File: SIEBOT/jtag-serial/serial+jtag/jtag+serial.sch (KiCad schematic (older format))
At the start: 26 parts, among them J1 USB_2, K1 CONN_3, K2 CONN_3, P1 CONN_14, P2 CONN_14, U1 93LC46BT-I/OT, U2 FT2232D, X1 CRYSTAL

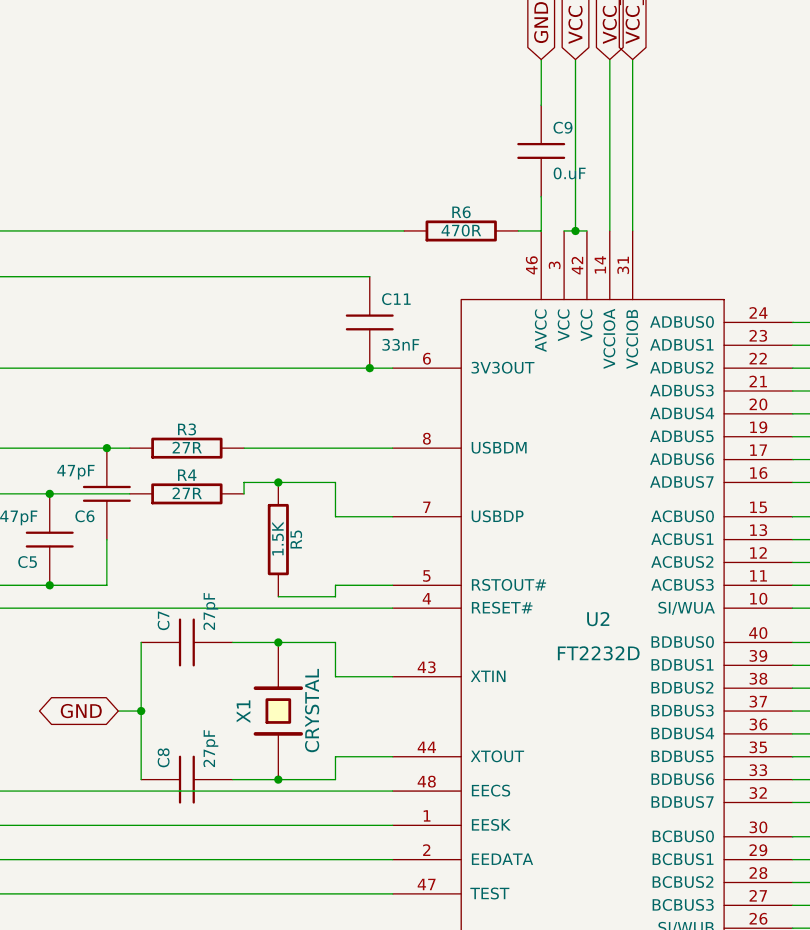
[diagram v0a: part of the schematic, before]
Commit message: Agregada BOM con referencias a Digikey. Corregido enpaquetado ferrita y valores condensadores carga del cristal. Signed-off-by: Erwin Lopez <erwinkendo@gmail.com>
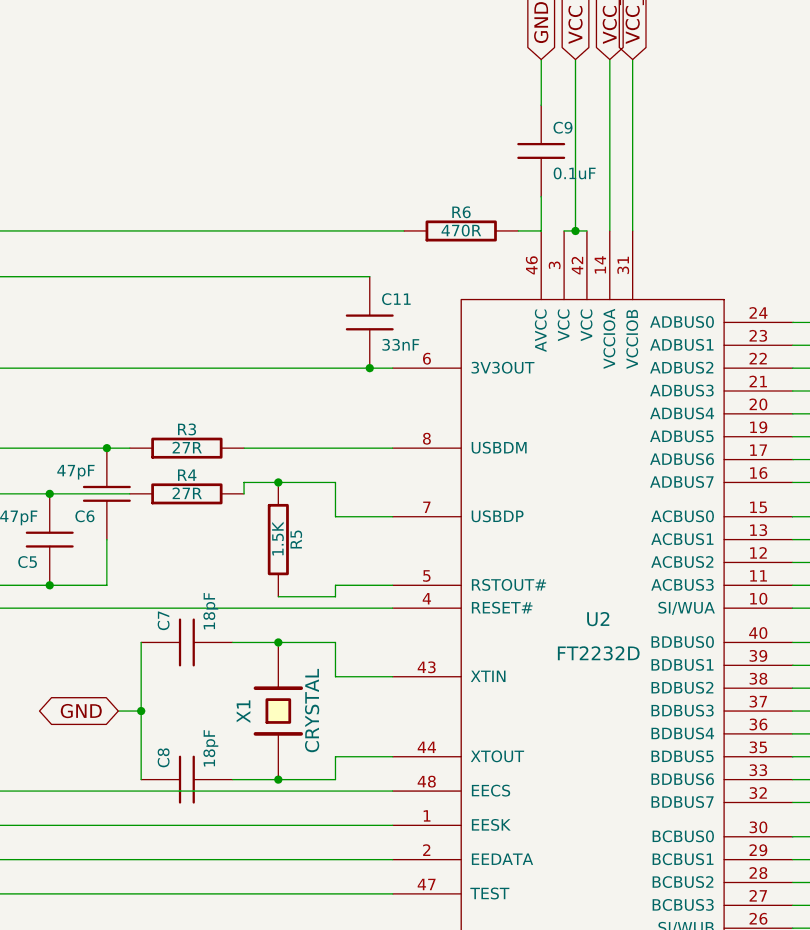
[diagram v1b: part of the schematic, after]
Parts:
- C7, C8: value 27pF -> 18pF
- C9: value 0.uF -> 0.1uF
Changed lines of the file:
@@
-EESchema Schematic File Version 2  date mar 03 abr 2012 00:18:22 COT
+EESchema Schematic File Version 2  date mar 10 abr 2012 00:47:13 COT
 LIBS:power
 LIBS:device
@@
 Sheet 1 1
 Title ""
-Date "3 apr 2012"
+Date "10 apr 2012"
 Rev ""
 Comp ""
@@
 P 7750 1700
 F 0 "C9" H 7800 1800 50  0000 L CNN
-F 1 "0.uF" H 7800 1600 50  0000 L CNN
+F 1 "0.1uF" H 7800 1600 50  0000 L CNN
 	1    7750 1700
 	1    0    0    -1
@@
 P 6200 4450
 F 0 "C8" H 6250 4550 50  0000 L CNN
-F 1 "27pF" H 6250 4350 50  0000 L CNN
+F 1 "18pF" H 6250 4350 50  0000 L CNN
 	1    6200 4450
 	0    -1   -1   0
@@
 P 6200 3850
 F 0 "C7" H 6250 3950 50  0000 L CNN
-F 1 "27pF" H 6250 3750 50  0000 L CNN
+F 1 "18pF" H 6250 3750 50  0000 L CNN
 	1    6200 3850
 	0    -1   -1   0
